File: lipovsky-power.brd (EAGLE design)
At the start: 57 x 32 mm, 103 parts, among them J1 M04-929J, J2 M04-929J, J3 M04-929J, J4 M04-929J, Q1 NMOS30V_30A, Q11 NMOS40V_10A, Q12 NMOS40V_10A, Q14 NMOS40V_10A, Q15 NMOS40V_10A, Q16 NMOS40V_10A, Q18 NMOS40V_10A, Q2 2NMOS30V_0.1A, Q21 PMOS30V_11A, Q22 PMOS30V_11A, Q23 NMOS40V_10A, Q24 NMOS40V_10A, Q25 PMOS30V_11A, Q26 PMOS30V_11A, Q27 NMOS40V_10A, Q28 NMOS40V_10A, Q3 2PMOS50V_0.17A, Q31 PMOS30V_11A, Q32 PMOS30V_11A, Q33 PMOS30V_11A, Q34 PMOS30V_11A, Q35 PMOS30V_11A, Q36 PMOS30V_11A, Q37 PMOS30V_11A, Q38 PMOS30V_11A, Q4 2PMOS50V_0.17A, Q41 PMOS30V_11A, Q42 PMOS30V_11A, Q43 PMOS30V_11A, Q44 PMOS30V_11A, Q45 PMOS30V_11A, Q46 PMOS30V_11A, Q47 PMOS30V_11A, Q48 PMOS30V_11A, Q5 2NMOS30V_0.1A, Q51 PMOS30V_11A, Q52 PMOS30V_11A, Q53 PMOS30V_11A, Q54 PMOS30V_11A, Q55 PMOS30V_11A, Q56 PMOS30V_11A, Q57 PMOS30V_11A, Q58 PMOS30V_11A, Q62 PMOS30V_11A, Q64 PMOS30V_11A, Q66 PMOS30V_11A, Q68 PMOS30V_11A, T1 TFORM_4_4311_4A4, U1 DG508BEN-T1-GE4, U2 DG508BEN-T1-GE4, U3 74HC595, U4 LTC3805-5IDD, U5 TC1240A, U6 AR30N60PPA-13

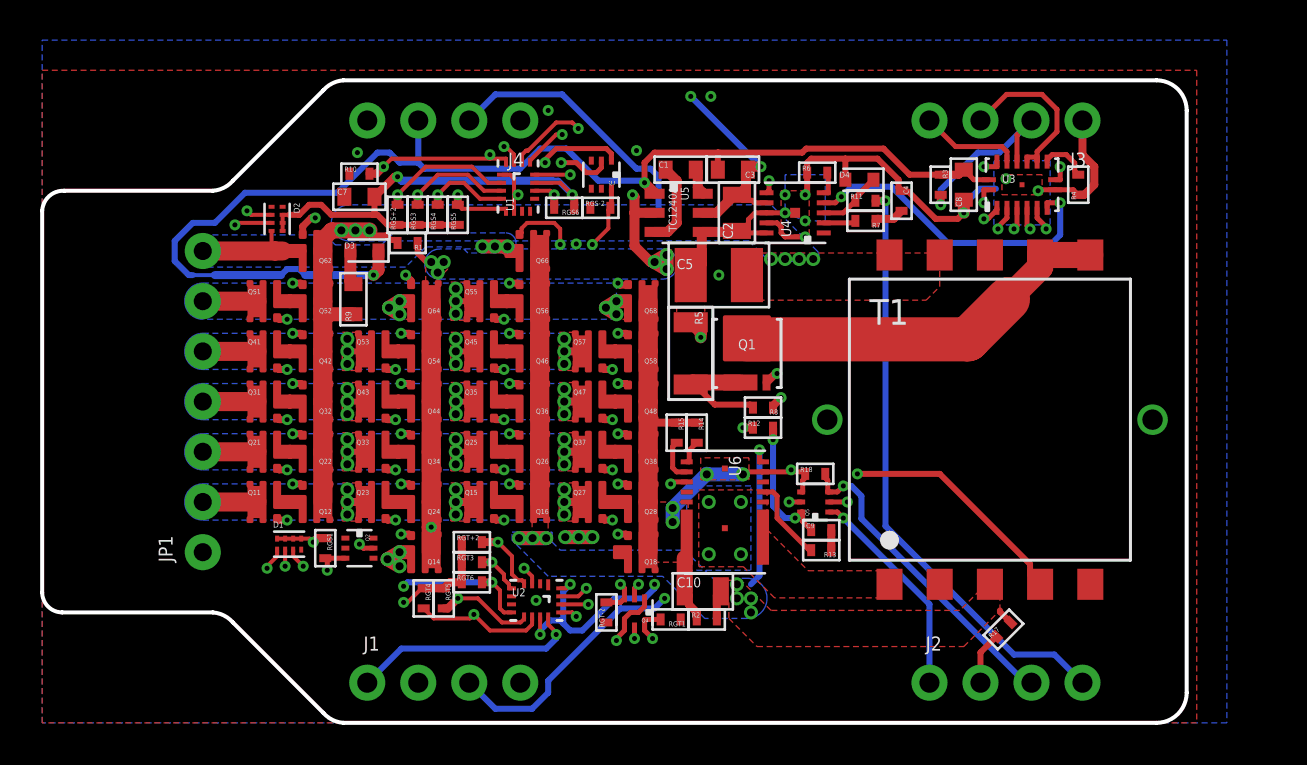
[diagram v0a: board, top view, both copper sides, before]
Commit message: moving boosters
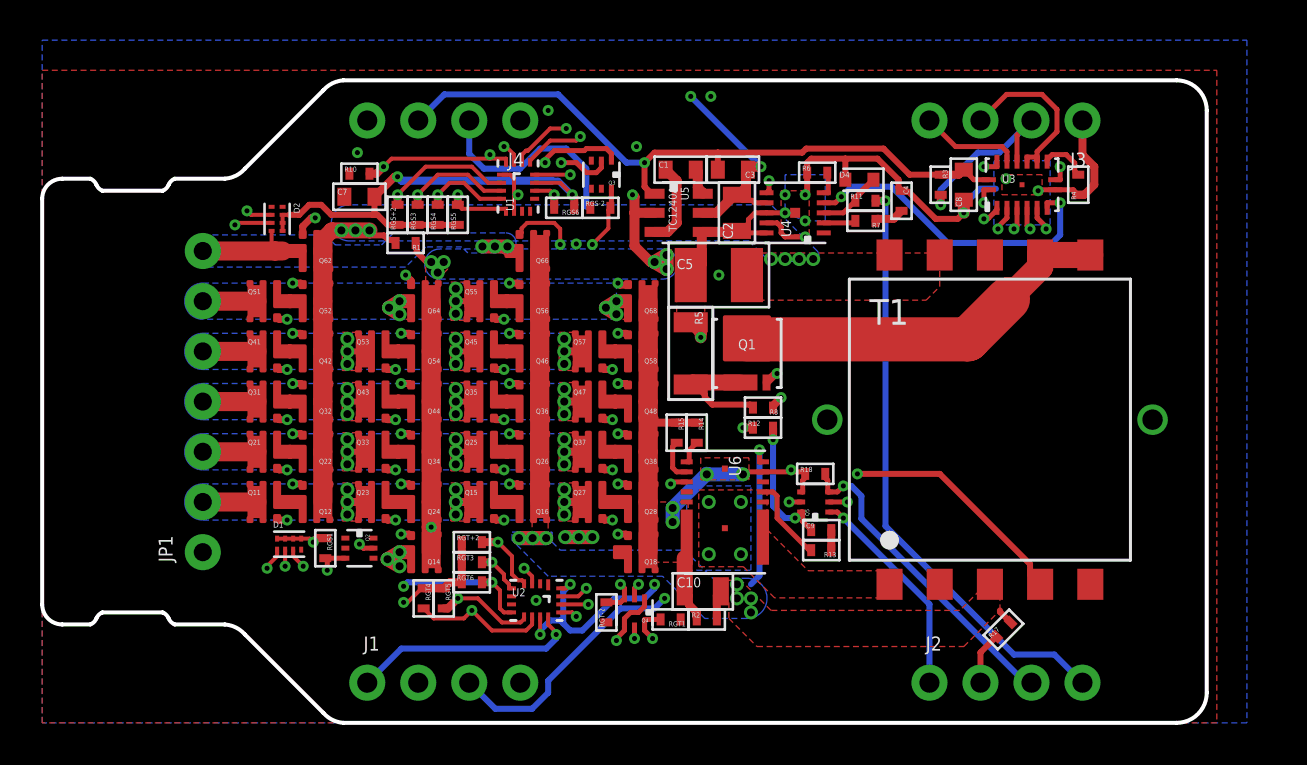
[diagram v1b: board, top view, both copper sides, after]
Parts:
- removed D3: D_SCH20V_0.5A, dubec:SOD523+
- removed R9: RES2_10, dubec:0603
- moved R1 0.10 mm to (18.1, 23.9)
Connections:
- removed net N$11: D3.A, R9.2
- net S+: no longer R9.1
- net VCC: no longer D3.C
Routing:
- net VCC: track 62.4 -> 34.2 mm, vias 2 -> 1
- net S+: track 39.2 -> 35.0 mm
- net N$11: track 1.74 -> 0.00 mm
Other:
- board size 57 x 32 mm -> 58 x 32 mm
- board text added: "5.8cm"
- board text removed: "5.7cm"

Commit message: .
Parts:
- removed C1, C3: CAP4.7U_10V, dubec:0603
- removed U5: TC1240A, dubec:SOT-23-6
- moved C2 3.80 mm to (30.8, 25.4)
- moved U4 3.20 mm to (34.3, 25.4)
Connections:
- removed net N$8: C1.2, U5.6
- removed net N$9: C1.1, U5.3
- net S-: no longer U5.2, U5.4
- net VCC: no longer C3.2, U5.1
- net VCC_REG: no longer C3.1, U5.5
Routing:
- net S-: track 116.2 -> 102.5 mm
- net N$9: track 4.16 -> 0.00 mm
- net VCC_REG: track 41.5 -> 37.7 mm
- net N$5: track 25.5 -> 28.7 mm
- net RUN_REG: track 15.9 -> 19.0 mm
- net VCC: track 34.2 -> 31.5 mm
- net N$1: track 3.25 -> 1.42 mm
- net N$12: track 1.62 -> 0.00 mm
- net N$6: track 13.5 -> 11.9 mm
- net N$8: track 1.34 -> 0.00 mm
- net N$3: track 1.25 -> 0.07 mm
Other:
- board size 58 x 32 mm -> 59 x 32 mm
- board text added: "5.9cm"
- board text removed: "5.8cm"

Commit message: .
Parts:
- moved U4 1.90 mm to (36.2, 25.4)
- moved C2 1.90 mm to (32.7, 25.4)
- moved D4 1.83 mm to (38.9, 27.4)
- moved R6 1.80 mm to (36.8, 27.4)
- moved C4 1.64 mm to (41.5, 25.0), turned to 180 degrees
- moved R11 1.30 mm to (39.7, 26.0)
- moved R7 1.30 mm to (39.7, 25.0)
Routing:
- net S-: track 102.5 -> 118.1 mm
- net N$5: track 28.7 -> 22.4 mm
- net N$1: track 1.42 -> 3.39 mm
- net RUN_REG: track 19.0 -> 17.2 mm
- net N$12: track 0.00 -> 1.62 mm
- net N$3: track 0.07 -> 1.27 mm
- net N$17: track 1.51 -> 0.80 mm
- net N$6: track 11.9 -> 12.6 mm
- net FB: track 29.7 -> 30.3 mm

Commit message: .
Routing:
- net VCC_REG: track 37.8 -> 36.0 mm
- net BATT-: vias 15 -> 34

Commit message: .
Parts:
- removed Q11, Q15: NMOS40V_10A, dubec:6-POWERWDFN
- moved RGT1 1.41 mm to (32.3, 4.15)
- moved R2 0.80 mm to (32.3, 5.15)
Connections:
- removed net SS+1: Q11.S, Q12.S
- removed net ST+1: Q15.S, Q16.S
- net C1: now also Q12.S, Q16.S; no longer Q11.D, Q15.D
- net GS1: no longer Q11.G
- net GT1: no longer Q15.G
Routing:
- net C1: track 12.9 -> 15.7 mm
- net GT1: track 19.0 -> 16.9 mm, vias 4 -> 3
- net GS1: track 14.5 -> 12.5 mm, vias 4 -> 3
- net GT4: track 31.5 -> 33.4 mm
- net GT+2: track 20.8 -> 22.5 mm
- net C4+: track 65.1 -> 63.5 mm
- net !EN_S1: track 65.9 -> 64.4 mm
- net SS+1: track 1.28 -> 0.00 mm
- net ST+1: track 1.27 -> 0.00 mm
- net T+: track 32.1 -> 31.1 mm
- net C2: track 21.2 -> 22.1 mm
- net GT3: track 22.1 -> 22.7 mm
- net GT5: track 32.6 -> 33.2 mm

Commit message: .
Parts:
- added R9: RES5.9K_16, dubec:0402
- R17: value RES402_16 -> RES330_16
- R18: value RES5.1K_16 -> RES1K_16
- moved R8 11.4 mm to (30.6, 25.8)
- moved C2 0.30 mm to (32.4, 25.4)
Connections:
- net RUN_REG renamed EN_FLYBACK
- net VCC renamed +5V
- net VCC_REG renamed +8V
- new net N$4: R9.1, U4.8
- net S-: no longer U4.8
- net SENSE: now also R9.2
- net SFB: no longer J1.3
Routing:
- net SFB: track 26.8 -> 7.71 mm, vias 3 -> 2
- net N$6: track 12.6 -> 5.19 mm
- net SENSE: track 6.11 -> 12.7 mm, vias 0 -> 2
- net N$4: track 0.00 -> 4.49 mm
- net S-: track 118.1 -> 114.7 mm, vias 19 -> 18
- net BATT-: vias 34 -> 35

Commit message: .
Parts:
- moved R17 21.1 mm to (26.8, 3.70), turned to 90 degrees
- moved RGT-2 1.82 mm to (27.8, 3.70)
- moved Q4 0.30 mm to (29.5, 5.20)
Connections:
- net BATT-: now also D2.1, D2.8, J1.4
- net Q7S: now also J1.3; no longer J1.4
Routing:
- net OPTO_A: track 2.62 -> 21.1 mm, vias 0 -> 1
- net T+: track 31.1 -> 37.7 mm
- net Q7S: track 44.5 -> 47.1 mm
- net GT-2: track 8.84 -> 10.3 mm
- net N$18: track 6.82 -> 7.39 mm
- removed copper zone on layer 1, net N$18

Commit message: .
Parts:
- added U$1: (no value), dubec:TF-EMBLEM
- J1, J2, J3, J4: device dubec:1X04 -> dubec:1X04_929J
- moved R2 1.20 mm to (33.5, 5.15)
- moved RGT1 1.20 mm to (33.5, 4.15)
- moved C4 0.10 mm to (41.6, 25.0)
- moved R11 0.10 mm to (39.8, 26.0)
- moved R7 0.10 mm to (39.8, 25.0)
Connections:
- net BATT-: now also Q2.1, Q2.2, Q2.6, Q3.4, Q3.5; no longer J1.4
- net Q7S: no longer J1.3
- net T+: now also J1.4
- net T-: now also J1.3
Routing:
- net Q7S: track 47.1 -> 0.00 mm, vias 1 -> 0
- net T-: track 43.9 -> 54.9 mm, vias 6 -> 5
- net T+: track 37.7 -> 39.8 mm
- net C1: track 15.7 -> 17.6 mm
- net GT1: track 17.2 -> 18.4 mm
- net S-: track 114.5 -> 115.1 mm
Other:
- board text added: "LiPovsky Balalaika"
- board text added: "Proto-1 2016-xx-xx"
- board text added: "TURBOfunction.com/fpv"
